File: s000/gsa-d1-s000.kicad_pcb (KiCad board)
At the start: 2 copper layers, 99.7 x 33 mm, 29 parts, among them J201 CONN-2, J202 CONN-4, J203 CONN-2, Q201 2N7000, Q202 2N7000, Q203 2N7000, Q204 2N7000, Q205 2N7000, SW201 SP-PUSH, SW202 SP-PUSH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

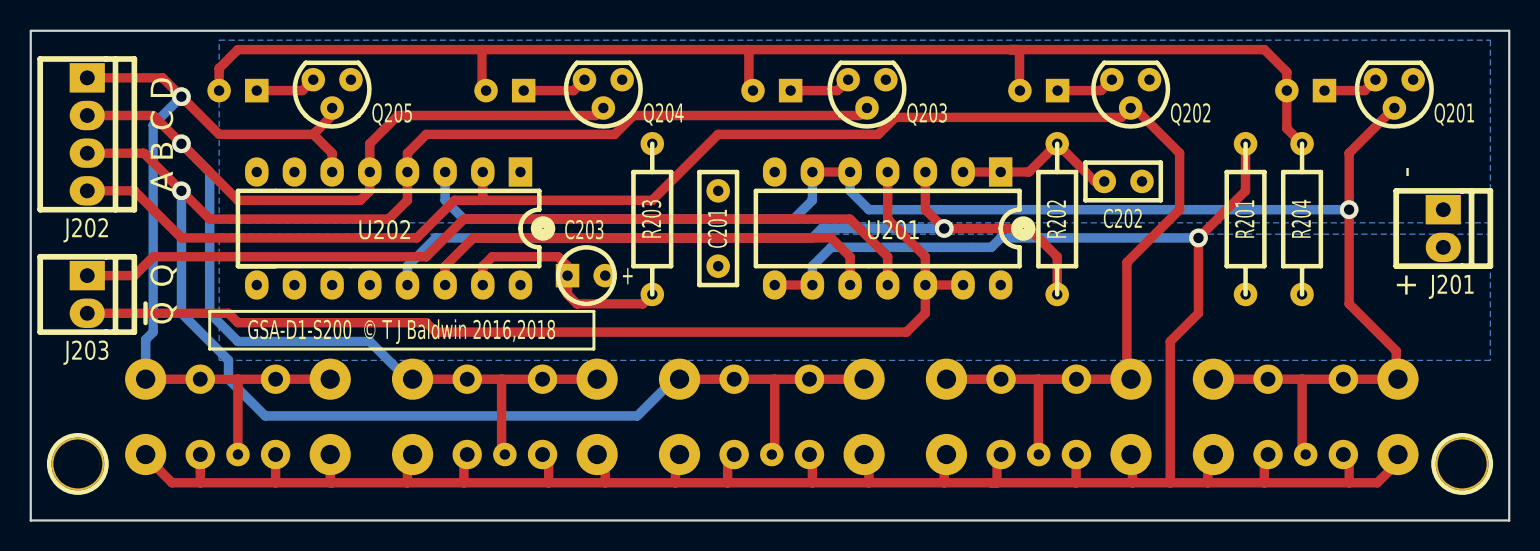
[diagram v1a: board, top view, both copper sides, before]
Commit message: Updated to use KiCad v5
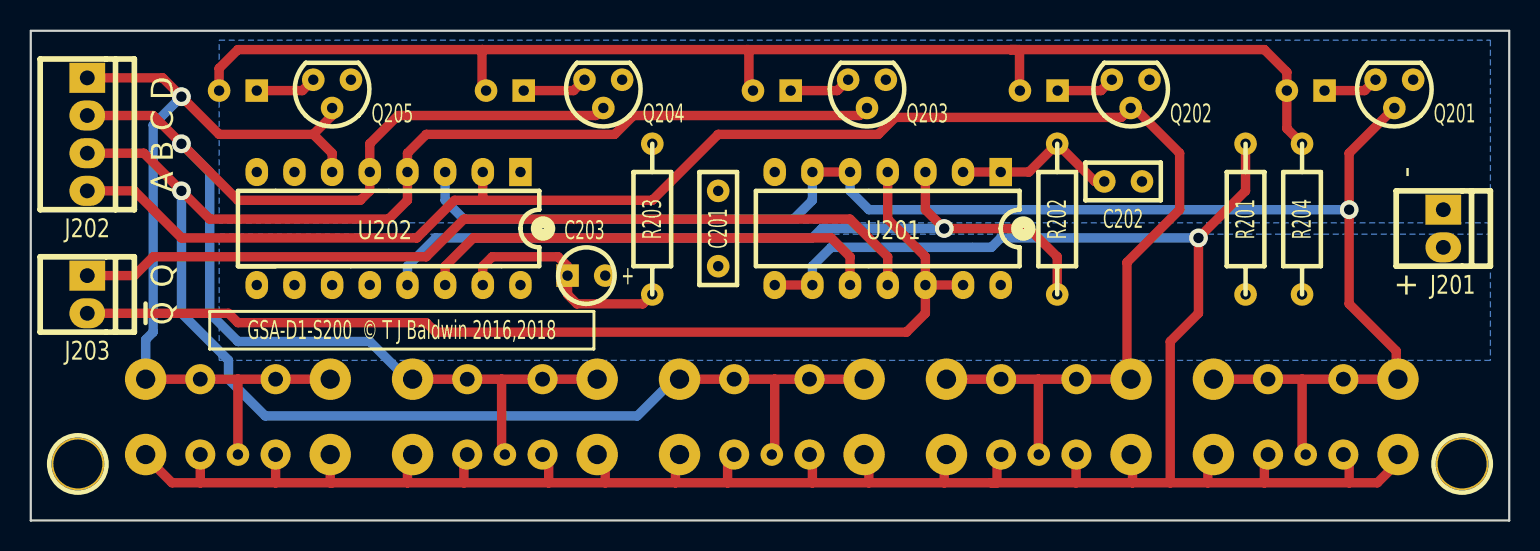
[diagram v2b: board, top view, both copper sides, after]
